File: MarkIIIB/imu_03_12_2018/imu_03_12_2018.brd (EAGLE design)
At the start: 16 x 19.9 mm, 15 parts, among them P301 502585-0470, U301 BNO055

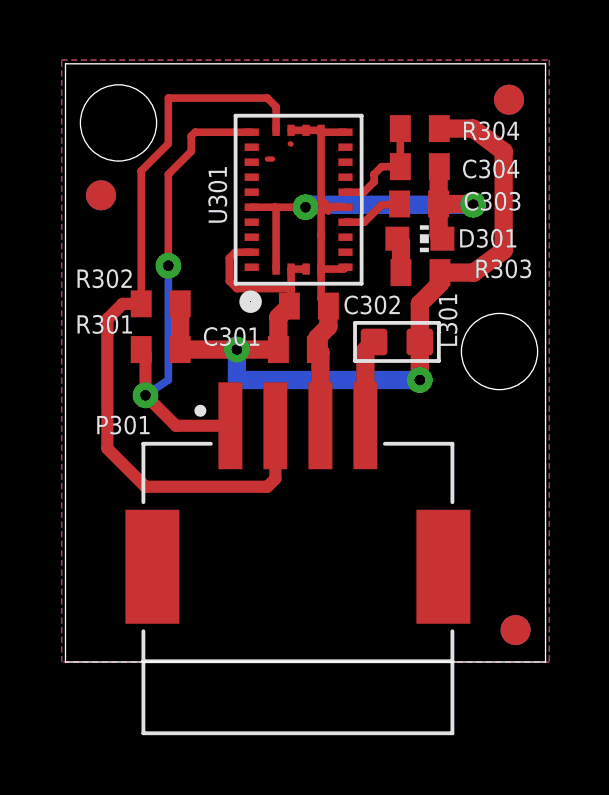
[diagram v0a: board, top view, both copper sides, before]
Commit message: Add Part Number ROllup Spreadsheets
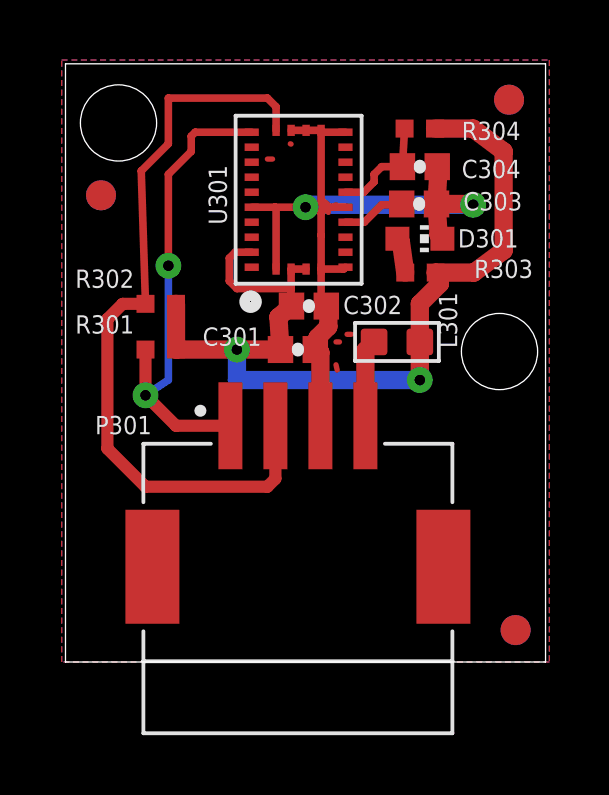
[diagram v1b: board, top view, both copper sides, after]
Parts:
- C301, C302, C303, C304: device rcl:C0402 -> PatternAgents-ProtoPads:0402-CAP
- R301, R302, R303, R304: device rcl:R0402 -> PatternAgents-ProtoPads:EIA-0402
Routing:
- net GND: track 28.1 -> 28.9 mm
- net VDD: track 30.9 -> 31.5 mm
